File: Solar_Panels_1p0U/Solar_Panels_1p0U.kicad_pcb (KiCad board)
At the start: 2 copper layers, 92 x 82 mm, 46 parts, among them J1 5040500891

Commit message: Kicad 9.0 PCB UPDATE
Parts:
- D3, D4, D5, D6, D7, D8, D9: moved to F.Cu
- SC1, SC10, SC11, SC12, SC13, SC14, SC15, SC16, SC17, SC18, SC19, SC2, SC20, SC21, SC22, SC23, SC24, SC25, SC26, SC27, SC3, SC4, SC5, SC6, SC7, SC8, SC9: footprint Solar Panels Library:Trisolx Wings -> Solar Panels Library:TrisolX Solar Wings
- moved D7 33.5 mm to (54.5, 91.0)
- moved D3 20.9 mm to (94.2, 59.0)
- moved D8 18.7 mm to (56.8, 81.2), turned to 0 degrees
- moved D4 17.7 mm to (90.0, 59.0)
- moved D5 15.9 mm to (85.2, 59.0)
- moved D6 13.2 mm to (79.0, 59.0)
- moved D1 9.65 mm to (126.5, 92.0)
- moved D2 7.95 mm to (127.5, 81.0)
- moved D9 7.42 mm to (59.0, 75.2)
- moved D10 6.25 mm to (129.2, 107.0), turned to -90 degrees
- moved SC3 3.37 mm to (137.0, 129.2)
- moved SC2 2.22 mm to (136.8, 107.8)
- moved SC14 1.58 mm to (97.2, 106.1)
- moved SC23 1.56 mm to (73.0, 106.1)
- moved SC22 1.55 mm to (73.2, 75.5)
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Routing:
- net Net-(D1-A): track 51.8 -> 0.00 mm
- net +VDC: track 43.7 -> 0.00 mm, vias 6 -> 0
- net Net-(SC4--): track 43.4 -> 0.00 mm
- net Net-(SC1--): track 41.6 -> 0.00 mm
- net Net-(SC13--): track 40.7 -> 0.00 mm
- net Net-(SC19--): track 40.4 -> 0.00 mm
- net Net-(SC16--): track 40.4 -> 0.00 mm
- net Net-(SC7--): track 40.3 -> 0.00 mm
- net Net-(SC22--): track 40.2 -> 0.00 mm
- net Net-(SC10--): track 40.0 -> 0.00 mm
- net Net-(D2-A): track 15.8 -> 0.00 mm
- net Net-(SC26--): track 15.3 -> 0.00 mm
- net Net-(SC23--): track 15.3 -> 0.00 mm
- net Net-(SC20--): track 15.1 -> 0.00 mm
- net Net-(SC17--): track 14.8 -> 0.00 mm
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
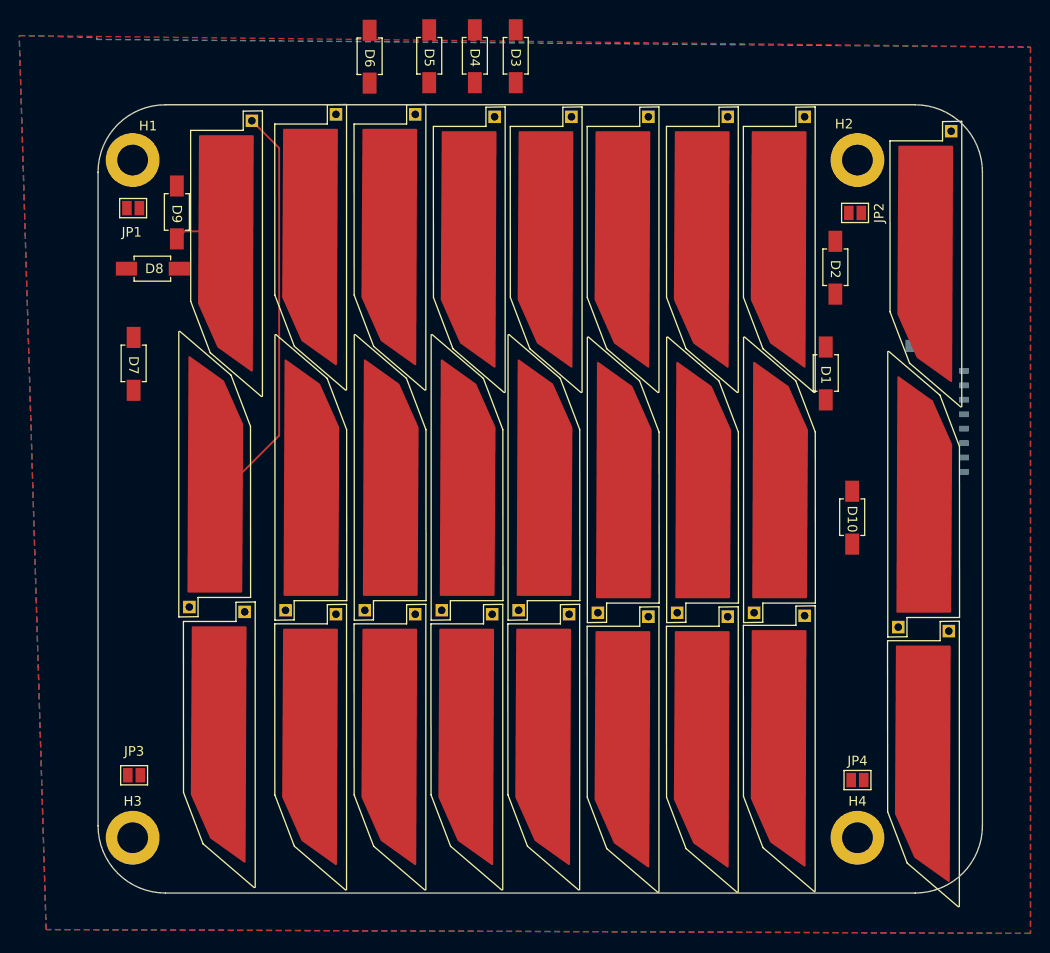
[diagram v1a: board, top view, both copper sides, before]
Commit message: Fixed diode placement and rerouted
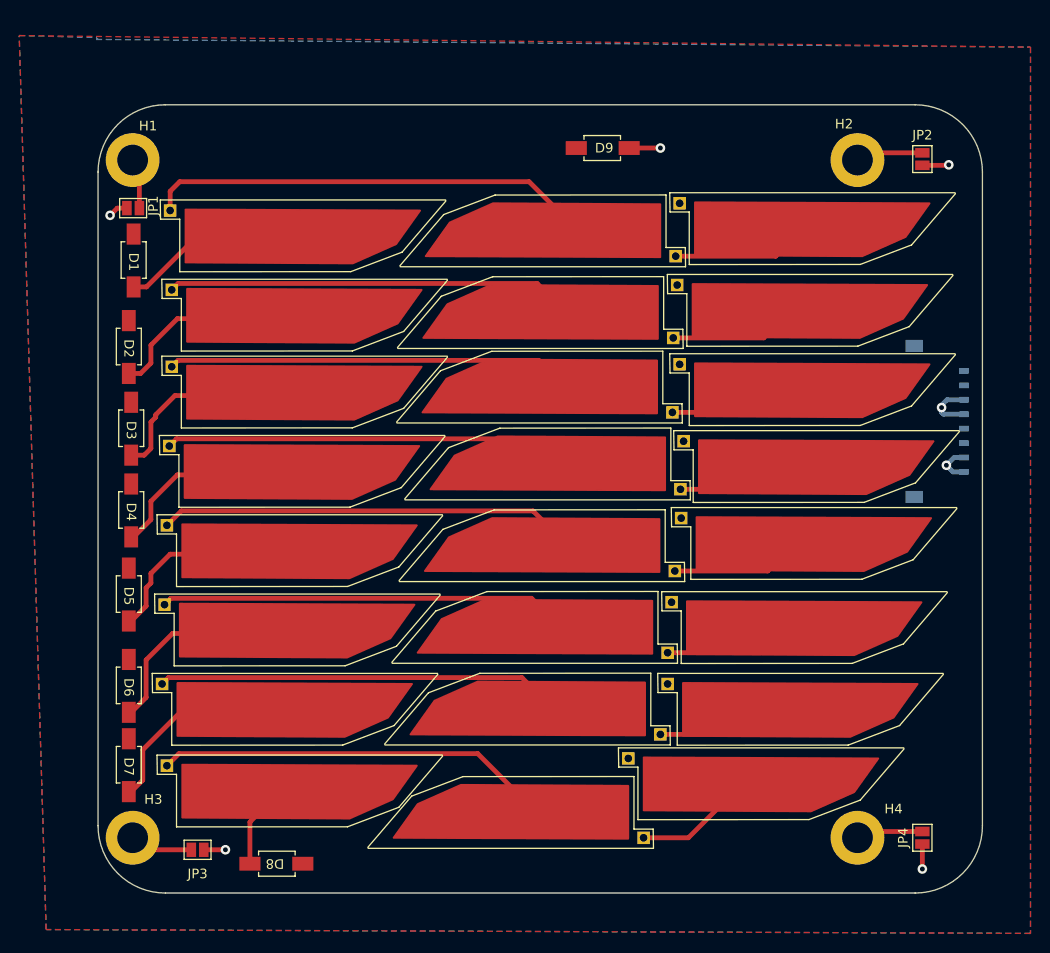
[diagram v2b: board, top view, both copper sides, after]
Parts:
- removed the D9 at (59.0, 75.2)
- removed SC25, SC26, SC27: Solar_Cell, Solar Panels Library:TrisolX Solar Wings
- moved D2 74.0 mm to (54.0, 89.2)
- moved D1 73.0 mm to (54.5, 80.2)
- moved D6 70.1 mm to (54.0, 124.5)
- moved SC1 68.3 mm to (69.0, 77.5), turned to -90 degrees
- moved D5 64.1 mm to (54.0, 115.0)
- moved D8 62.8 mm to (69.5, 142.8), turned to 180 degrees
- moved SC22 59.9 mm to (68.7, 135.2), turned to -90 degrees
- moved D4 59.3 mm to (54.2, 106.2)
- moved D3 55.7 mm to (54.2, 97.8)
- moved SC3 54.6 mm to (122.0, 76.8), turned to -90 degrees
- moved SC4 53.8 mm to (69.2, 85.8), turned to -90 degrees
- moved SC19 53.0 mm to (68.2, 126.8), turned to -90 degrees
- moved SC7 48.3 mm to (69.2, 93.8), turned to -90 degrees
- moved SC16 47.8 mm to (68.4, 118.5), turned to -90 degrees
- moved SC2 47.4 mm to (100.6, 77.2), turned to 90 degrees
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- renumbered D10 to D9
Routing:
- net Net-(SC1--): track 0.00 -> 46.8 mm
- net Net-(SC13--): track 0.00 -> 43.3 mm
- net Net-(SC10--): track 0.00 -> 42.9 mm
- net Net-(SC25--): track 42.9 -> 0.00 mm
- net Net-(SC16--): track 0.00 -> 42.2 mm
- net Net-(SC4--): track 0.00 -> 42.1 mm
- net Net-(SC7--): track 0.00 -> 41.9 mm
- net Net-(SC19--): track 0.00 -> 41.8 mm
- net Net-(SC22--): track 0.00 -> 41.0 mm
- net Net-(D6-A): track 0.00 -> 20.9 mm
- net Net-(D7-A): track 0.00 -> 20.2 mm
- net Net-(D5-A): track 0.00 -> 20.0 mm
- net Net-(D3-A): track 0.00 -> 20.0 mm
- net Net-(D2-A): track 0.00 -> 19.4 mm
- net Net-(D4-A): track 0.00 -> 19.3 mm
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
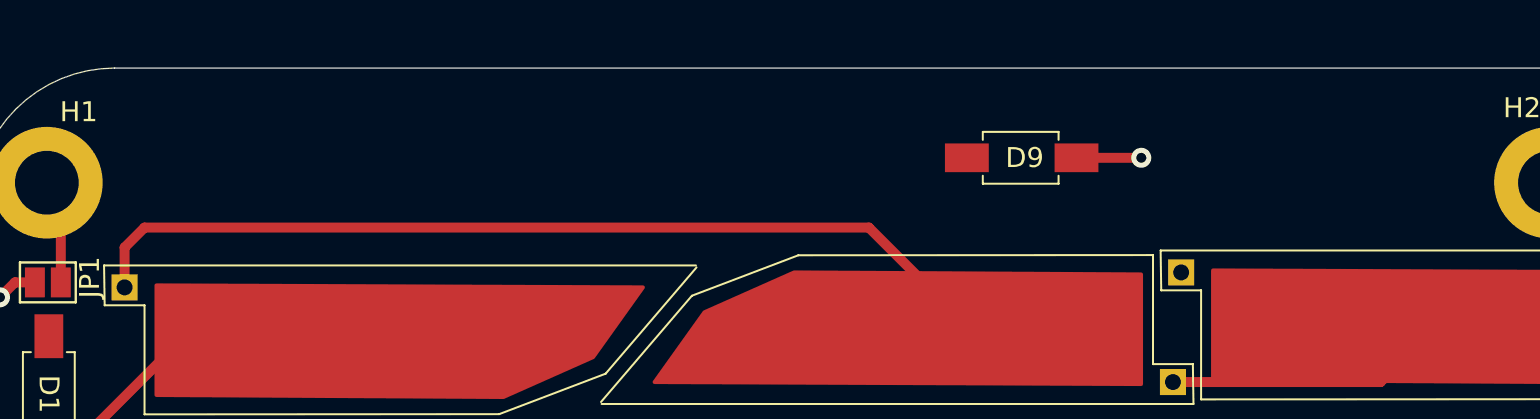
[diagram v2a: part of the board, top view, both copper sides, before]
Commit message: Add files via upload
Added logo, revision number, date, and label to PCB. Updated the revision date and revision number on the schematic and PCB
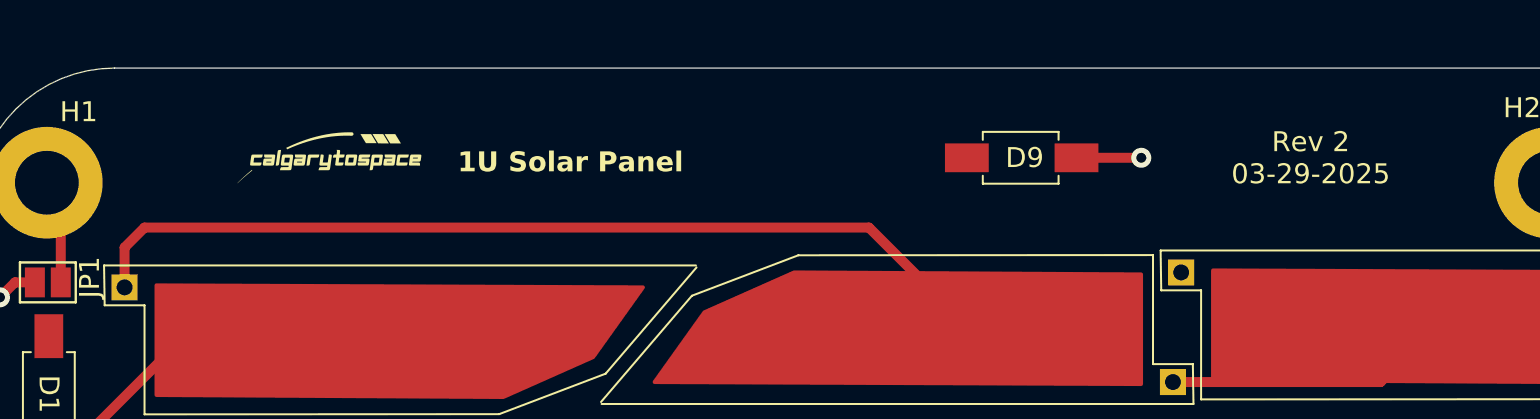
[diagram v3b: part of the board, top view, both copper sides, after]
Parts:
- added G***: LOGO, CTS:small_one, F.Cu at (68.7, 68.2)
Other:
- board text added: "1U Solar Panel"
- board text added: "Rev 2 03-29-2025"
